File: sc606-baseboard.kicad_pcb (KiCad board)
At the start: 6 copper layers, 100 x 90 mm, 465 parts, among them IC1 TPS54561DPRT, IC2 TPS7A0518PDBVT, IC3 HD3SS3220, IC4 HD3SS3220, J1 PJ-202A, J10 WE_632723300011, J11 USB-A3-C31-D-RA-CS1, J12 U_FL-R-SMT-1_10_, J13 USB-A3-C31-D-RA-CS1, J2 WE_68715014522, J3 F52R-1A7H1-11020, J4 46756-1001, J5 U_FL-R-SMT-1_10_, J6 U_FL-R-SMT-1_10_, J7 DM3AT-SF-PEJM5, J8 693022010811, J9 0473460001, M1 SC606T, Q1 BSS138APW, Q2 BSS138-7-F, Q3 BSS138APW, Q4 BSS138APW, Q5 BSS138APW, Q6 BSS138APW, Q7 BSS138-7-F, Q8 BSS138-7-F, SW1 1X03, U1 AP62301WU-7, U10 NCP163ASN330T1G, U11 EMIF06-MSD02N16, U12 FSUSB30MUX, U13 FT232RQ-REEL, U15 USB57442G, U2 AP62301WU-7, U3 AP62301WU-7, U4 74LVC1G123GN, U5 NTS0102GT, U6 PCA9547BS, U7 LT9611UXC, U8 NTS0102GT, U9 TPD13S523PWR, Y1 ABM8G-24.000MHZ-18-D2Y-T, Y2 ABM8G-25.000MHZ-B4Y-T

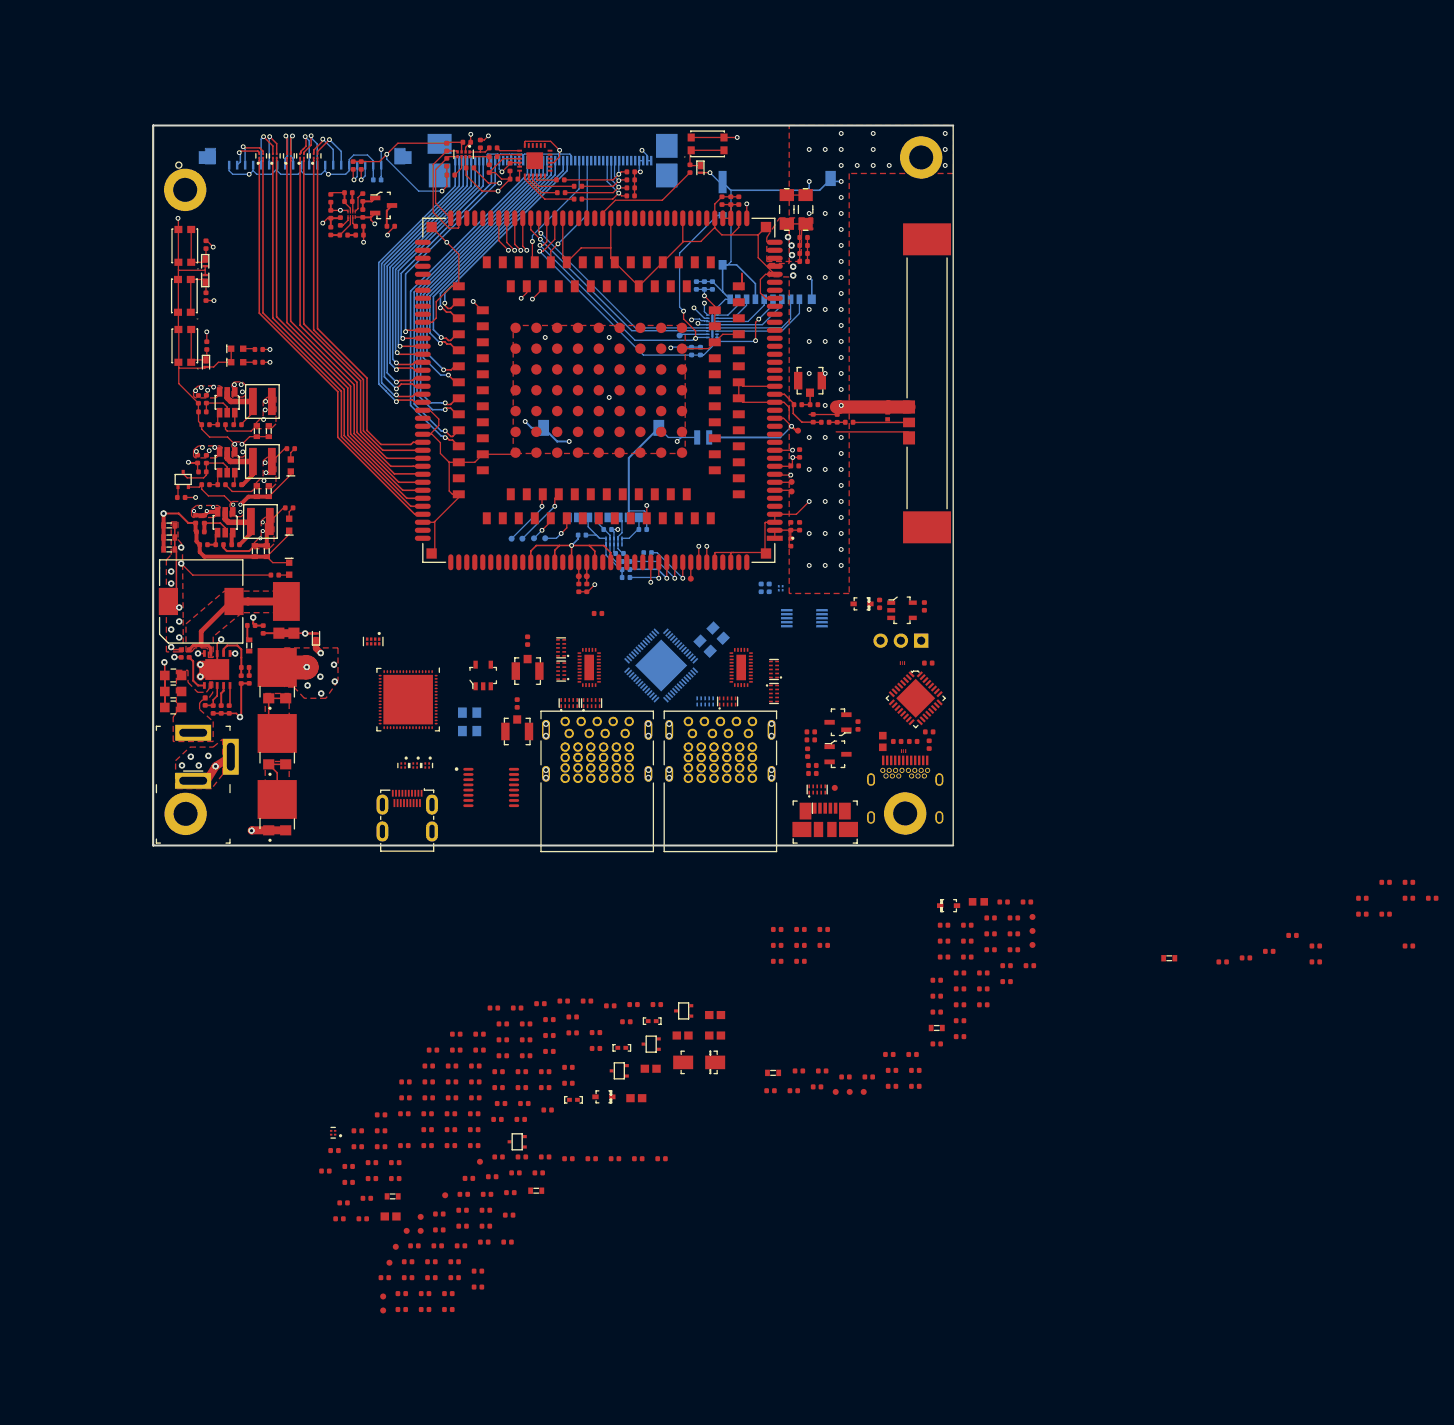
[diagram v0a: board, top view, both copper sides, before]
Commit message: Started rearrangement of components. USB connectors changed to 2xUSB-C
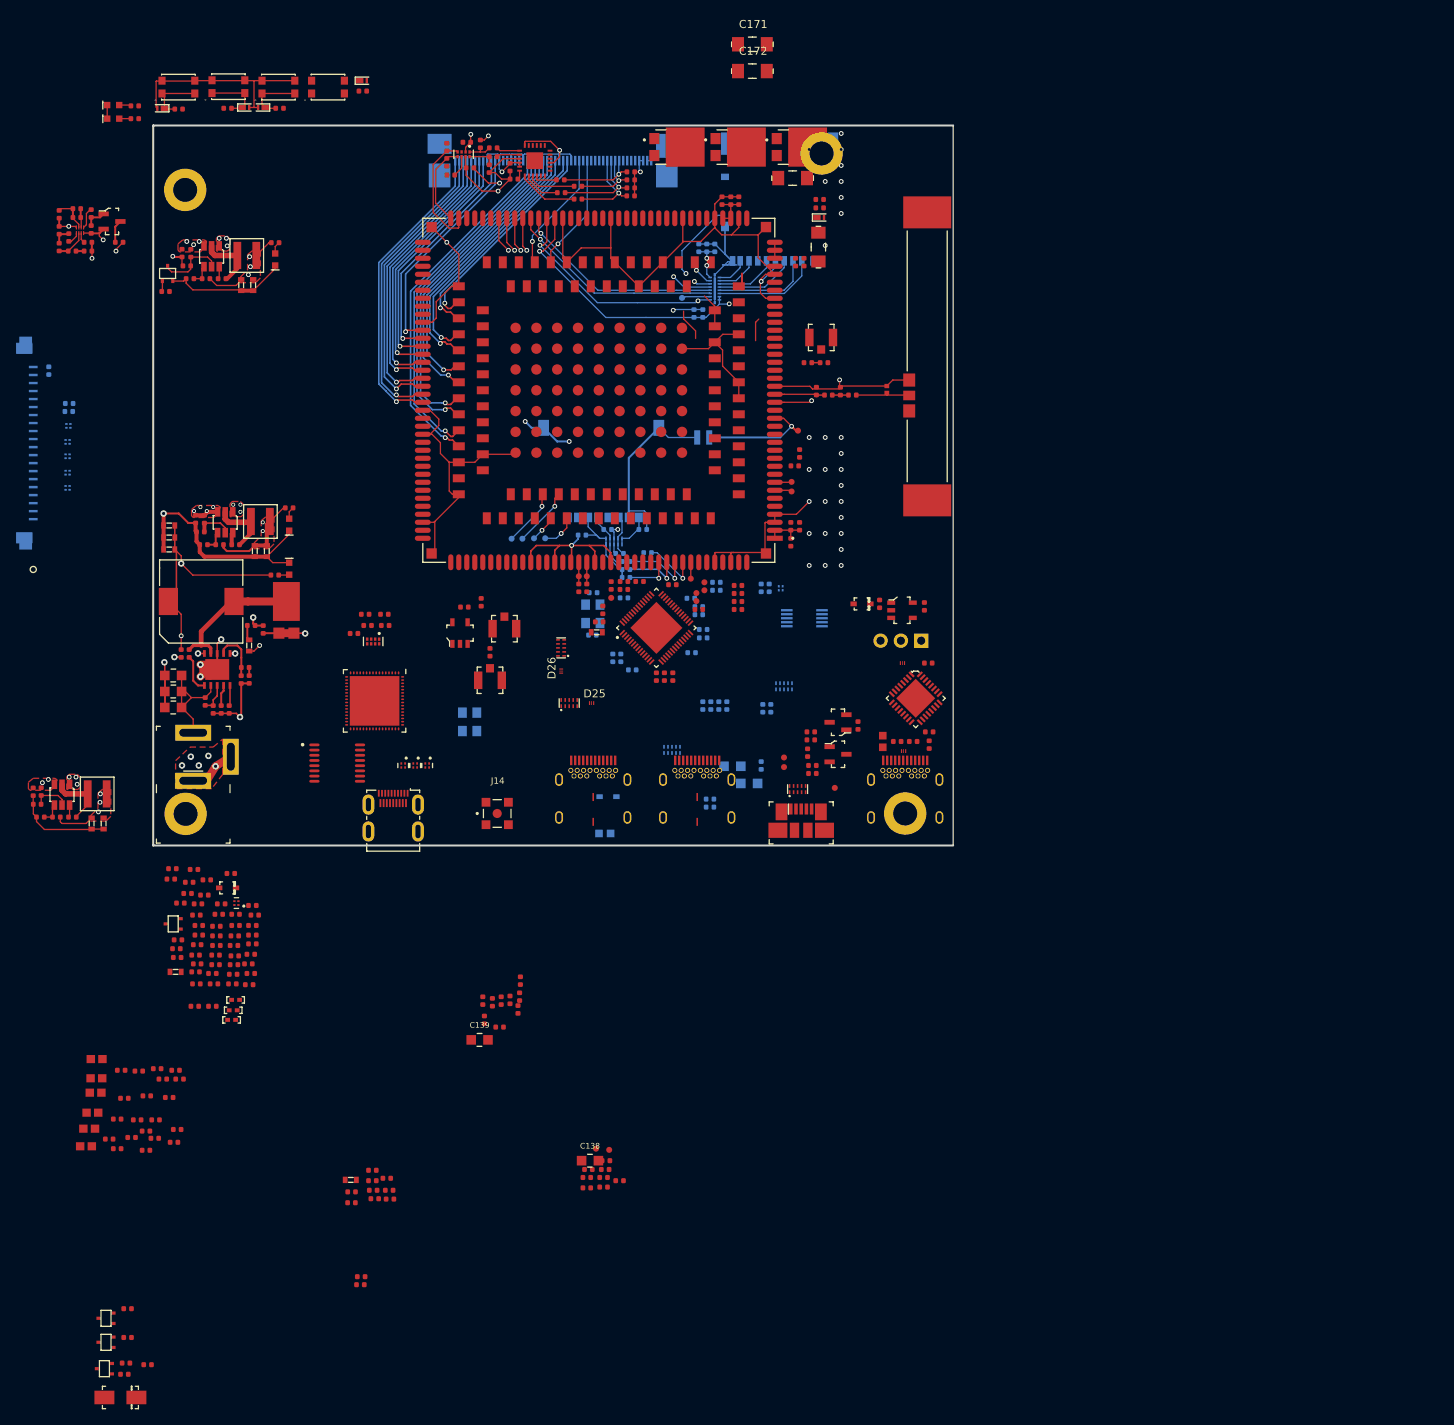
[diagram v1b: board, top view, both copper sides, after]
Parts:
- removed C142, C143, C144, C145, C153, C154, C155, C156, C157, C159, C160, C161, C162, C163, C164, C165, C166: C_100n_0402, sc606-baseboard-footprints:0402-cap
- removed C146, C158: C_47u_0603, sc606-baseboard-footprints:0603-cap
- removed C152: C_10u_0402, sc606-baseboard-footprints:0402-cap
- removed D29, D30: PUSB3F96X_PASS, sc606-baseboard-footprints:PUSB3F96X
- removed IC3, IC4: HD3SS3220, sc606-baseboard-footprints:RNH0030A
- removed R138, R143, R147, R148, R149, R150, R151, R152, R161: R_0R_0402, sc606-baseboard-footprints:0402-res
- removed R139, R140, R146, R153, R154: R_2k_0402, sc606-baseboard-footprints:0402-res
- removed R141, R159: R_909k_0402, sc606-baseboard-footprints:0402-res
- removed R142, R144, R160: R_200k_0402, sc606-baseboard-footprints:0402-res
- removed R145: R_10k_0402, sc606-baseboard-footprints:0402-res
- removed TP20, TP21, TP22, TP25, TP26, TP27: TP_SMD_0_75MM, sc606-baseboard-footprints:Testpoint_smd_0_75mm
- added C169: C_100u_0805, sc606-baseboard-footprints:0805-cap, B.Cu at (149.5, 122.2)
- added C170: C_100u_0805, sc606-baseboard-footprints:0805-cap, B.Cu at (147.4, 120.1)
- added C171: C_100u_1206, sc606-baseboard-footprints:1206-cap, F.Cu at (149.9, 29.9)
- added C172: C_100u_1206, sc606-baseboard-footprints:1206-cap, F.Cu at (149.9, 33.2)
- added J14: CONMMCX002-SMD-T, sc606-baseboard-footprints:LINX_CONMMCX002-SMD-T, F.Cu at (118.0, 126.0)
- C121, C122, C123, C124, C127, C129, C132, C133, C134, C135, C136, C137, C147, C148, C149, C150, C151, D24, D31, D32, FB2, L10, L11, L12, L8, L9, R119, R120, R155, R156, R157, R158, R55, R56: moved to B.Cu
- C138: value C_100n_0402 -> C_100u_0805; footprint sc606-baseboard-footprints:0402-cap -> sc606-baseboard-footprints:0805-cap
- C139: value C_10u_0402 -> C_100u_0805; footprint sc606-baseboard-footprints:0402-cap -> sc606-baseboard-footprints:0805-cap
- D25, D26: value PUSB3F96X_PASS -> PESD5V0C2BDFZ; footprint sc606-baseboard-footprints:PUSB3F96X -> sc606-baseboard-footprints:DFN0603-3
- J11, J13: value USB-A3-C31-D-RA-CS1 -> WE_632723300011; footprint sc606-baseboard-footprints:USB-A3-C31-D-RA-CS1 -> sc606-baseboard-footprints:WE_632723300011
- R130: value R_200k_0402 -> R_0R_0402
- R131: value R_10k_0402 -> R_0R_0402
- R132: value R_2k_0402 -> R_0R_0402
- R162: footprint antmicro-footprints:0402-res -> sc606-baseboard-footprints:0402-res
- U15: moved to F.Cu
- moved C89 135.8 mm to (101.0, 183.9)
- moved C91 134.2 mm to (100.9, 184.9)
- moved C96 133.2 mm to (104.5, 173.1)
- moved C93 132.8 mm to (104.6, 174.2)
- moved C87 130.2 mm to (104.2, 171.6)
- moved C95 127.8 mm to (102.4, 170.6)
- moved C101 121.5 mm to (102.4, 171.9)
- moved C98 119.2 mm to (102.5, 173.1)
- moved C99 118.6 mm to (99.8, 173.3)
- moved C103 114.1 mm to (118.3, 152.7)
- moved R93 113.0 mm to (99.8, 174.7)
- moved R92 113.0 mm to (102.7, 174.2)
- moved C94 110.8 mm to (129.4, 170.5)
- moved R94 106.0 mm to (99.7, 171.8)
- moved D3 96.5 mm to (140.5, 42.7), turned to 270 degrees
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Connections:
- C102 pad 1: /USB_HUB_Connectors/USB_C1_SS_C_TX2_N -> /USB_HUB_Connectors/USB_C1_SS_C_TX1_N
- C102 pad 2: /USB_HUB_Connectors/USB_C1_SS_TX2_N -> /USB_HUB_Connectors/USB_C1_SS_TX1_N
- C103 pad 2: /USB_HUB_Connectors/5V0_USB -> Net-(C103-Pad2)
- C138 pad 1: /USB_HUB_Connectors/USB_C1_SS_C_TX1_P -> GND
- C138 pad 2: /USB_HUB_Connectors/USB_C1_SS_TX1_P -> Net-(C103-Pad2)
- C139 pad 1: /USB_HUB_Connectors/5V0_USB -> GND
- C139 pad 2: GND -> Net-(C103-Pad2)
- C140 pad 1: Net-(C140-Pad1) -> /USB_HUB_Connectors/USB_C1_SS_C_TX2_N
- C140 pad 2: /USB_HUB_Connectors/USB_C1_SS_RX2_N -> /USB_HUB_Connectors/USB_C1_SS_TX2_N
- C141 pad 1: /USB_HUB_Connectors/USB_C1_SS_C_TX1_N -> /USB_HUB_Connectors/USB_C1_SS_C_TX2_P
- C141 pad 2: /USB_HUB_Connectors/USB_C1_SS_TX1_N -> /USB_HUB_Connectors/USB_C1_SS_TX2_P
- C151 pad 2: /USB_HUB_Connectors/5V0_USB -> Net-(C151-Pad2)
- C94 pad 1: /USB_HUB_Connectors/USB_C1_SS_C_TX2_P -> /USB_HUB_Connectors/USB_C1_SS_C_TX1_P
- C94 pad 2: /USB_HUB_Connectors/USB_C1_SS_TX2_P -> /USB_HUB_Connectors/USB_C1_SS_TX1_P
- D25 pad 1: /USB_HUB_Connectors/USB_A1_SS_TX_P -> /USB_HUB_Connectors/USB_C1_D_P
- D25 pad 2: /USB_HUB_Connectors/USB_A1_SS_TX_N -> /USB_HUB_Connectors/USB_C1_D_N
- D26 pad 1: /USB_HUB_Connectors/USB_C1_D_P -> /USB_HUB_Connectors/USB_C2_D_P
- D26 pad 2: /USB_HUB_Connectors/USB_C1_D_N -> /USB_HUB_Connectors/USB_C2_D_N
- D31 pad 1: /USB_HUB_Connectors/USB_C2_SS_RX2_P -> /USB_HUB_Connectors/USB_C2_SS_TX2_P
- D31 pad 10: /USB_HUB_Connectors/USB_C2_SS_RX2_P -> /USB_HUB_Connectors/USB_C2_SS_TX2_P
- D31 pad 2: /USB_HUB_Connectors/USB_C2_SS_RX2_N -> /USB_HUB_Connectors/USB_C2_SS_TX2_N
- D31 pad 4: /USB_HUB_Connectors/USB_C2_SS_TX2_P -> /USB_HUB_Connectors/USB_C2_SS_RX2_P
- D31 pad 5: /USB_HUB_Connectors/USB_C2_SS_TX2_N -> /USB_HUB_Connectors/USB_C2_SS_RX2_N
- D31 pad 6: /USB_HUB_Connectors/USB_C2_SS_TX2_N -> /USB_HUB_Connectors/USB_C2_SS_RX2_N
- D31 pad 7: /USB_HUB_Connectors/USB_C2_SS_TX2_P -> /USB_HUB_Connectors/USB_C2_SS_RX2_P
- D31 pad 9: /USB_HUB_Connectors/USB_C2_SS_RX2_N -> /USB_HUB_Connectors/USB_C2_SS_TX2_N
- D6 pad 2: /display module/SCL_HDMI -> /display module/LTtoHDMI_SCL
- D7 pad 2: /display module/SDA_HDMI -> /display module/LTtoHDMI_SDA
- D8 pad 2: /display module/CEC -> (no net)
- J10 pad A10: Net-(J10-PadA10) -> (no net)
- J10 pad A11: Net-(J10-PadA11) -> (no net)
- J10 pad A2: Net-(J10-PadA2) -> (no net)
- J10 pad A3: Net-(J10-PadA3) -> (no net)
- J10 pad A5: Net-(J10-PadA5) -> (no net)
- J10 pad A8: Net-(J10-PadA8) -> (no net)
- J10 pad B10: Net-(J10-PadB10) -> (no net)
- J10 pad B11: Net-(J10-PadB11) -> (no net)
- J10 pad B2: Net-(J10-PadB2) -> (no net)
- J10 pad B3: Net-(J10-PadB3) -> (no net)
- J10 pad B5: Net-(J10-PadB5) -> (no net)
- J10 pad B8: Net-(J10-PadB8) -> (no net)
- J11 pad A1: GND -> (no net)
- J11 pad A10: Net-(C140-Pad1) -> /USB_HUB_Connectors/USB_C1_SS_C_RX2_N
- J11 pad A11: Net-(C143-Pad1) -> /USB_HUB_Connectors/USB_C1_SS_C_RX2_P
- J11 pad B1: GND -> Net-(C103-Pad2)
- J11 pad B10: Net-(C142-Pad1) -> /USB_HUB_Connectors/USB_C1_SS_C_RX1_P
- J11 pad B11: Net-(C144-Pad1) -> /USB_HUB_Connectors/USB_C1_SS_C_RX1_N
- J11 pad B12: GND -> (no net)
- J13 pad A1: GND -> (no net)
- J13 pad B1: GND -> Net-(C151-Pad2)
- J13 pad B10: /USB_HUB_Connectors/USB_C2_SS_C_RX1_N -> /USB_HUB_Connectors/USB_C2_SS_C_RX1_P
- J13 pad B11: /USB_HUB_Connectors/USB_C2_SS_C_RX1_P -> /USB_HUB_Connectors/USB_C2_SS_C_RX1_N
- J13 pad B12: GND -> (no net)
- J2 pad 13: Net-(J2-Pad13) -> (no net)
- J2 pad 14: Net-(J2-Pad14) -> (no net)
- J2 pad 16: Net-(J2-Pad16) -> (no net)
- J2 pad 17: Net-(J2-Pad17) -> (no net)
- J2 pad 31: Net-(J2-Pad31) -> (no net)
- J2 pad 33: Net-(J2-Pad33) -> (no net)
- J2 pad 35: Net-(J2-Pad35) -> (no net)
- J2 pad 36: Net-(J2-Pad36) -> (no net)
- J2 pad 37: Net-(J2-Pad37) -> (no net)
- J2 pad 38: Net-(J2-Pad38) -> (no net)
- J2 pad 43: Net-(J2-Pad43) -> (no net)
- J2 pad 44: Net-(J2-Pad44) -> (no net)
- J2 pad 45: Net-(J2-Pad45) -> (no net)
- J2 pad 46: Net-(J2-Pad46) -> (no net)
- J8 pad C4: Net-(J8-PadC4) -> (no net)
- J8 pad C6: Net-(J8-PadC6) -> (no net)
- J8 pad C8: Net-(J8-PadC8) -> (no net)
- L10 pad 1: SoMtoDisplay_D1_N -> SoMtoDisplay_D1_P
- L10 pad 2: /display module/SoMtoDisplay_Ferr_D1_N -> /display module/SoMtoDisplay_Ferr_D1_P
- L10 pad 3: /display module/SoMtoDisplay_Ferr_D1_P -> /display module/SoMtoDisplay_Ferr_D1_N
- L10 pad 4: SoMtoDisplay_D1_P -> SoMtoDisplay_D1_N
- L11 pad 1: SoMtoDisplay_D0_N -> SoMtoDisplay_D0_P
- L11 pad 2: /display module/SoMtoDisplay_Ferr_D0_N -> /display module/SoMtoDisplay_Ferr_D0_P
- L11 pad 3: /display module/SoMtoDisplay_Ferr_D0_P -> /display module/SoMtoDisplay_Ferr_D0_N
- L11 pad 4: SoMtoDisplay_D0_P -> SoMtoDisplay_D0_N
- L12 pad 1: SoMtoDisplay_CLK_N -> SoMtoDisplay_CLK_P
- L12 pad 2: /display module/SoMtoDisplay_Ferr_CLK_N -> /display module/SoMtoDisplay_Ferr_CLK_P
- L12 pad 3: /display module/SoMtoDisplay_Ferr_CLK_P -> /display module/SoMtoDisplay_Ferr_CLK_N
- L12 pad 4: SoMtoDisplay_CLK_P -> SoMtoDisplay_CLK_N
- L8 pad 1: SoMtoDisplay_D3_N -> SoMtoDisplay_D3_P
- L8 pad 2: /display module/SoMtoDisplay_Ferr_D3_N -> /display module/SoMtoDisplay_Ferr_D3_P
- L8 pad 3: /display module/SoMtoDisplay_Ferr_D3_P -> /display module/SoMtoDisplay_Ferr_D3_N
- L8 pad 4: SoMtoDisplay_D3_P -> SoMtoDisplay_D3_N
- L9 pad 1: SoMtoDisplay_D2_N -> SoMtoDisplay_D2_P
- L9 pad 2: /display module/SoMtoDisplay_Ferr_D2_N -> /display module/SoMtoDisplay_Ferr_D2_P
- L9 pad 3: /display module/SoMtoDisplay_Ferr_D2_P -> /display module/SoMtoDisplay_Ferr_D2_N
- L9 pad 4: SoMtoDisplay_D2_P -> SoMtoDisplay_D2_N
- M1 pad 100: Net-(M1-Pad100) -> (no net)
- M1 pad 11: LDO10_2P8 -> (no net)
- M1 pad 113: Net-(M1-Pad113) -> (no net)
- M1 pad 114: Net-(M1-Pad114) -> (no net)
- M1 pad 126: Net-(M1-Pad126) -> (no net)
- M1 pad 127: Net-(M1-Pad127) -> (no net)
- M1 pad 13: Net-(M1-Pad13) -> (no net)
- M1 pad 136: Net-(M1-Pad136) -> (no net)
- M1 pad 137: Net-(M1-Pad137) -> (no net)
- M1 pad 138: Net-(M1-Pad138) -> (no net)
- M1 pad 139: Net-(M1-Pad139) -> (no net)
- M1 pad 14: Net-(M1-Pad14) -> (no net)
- M1 pad 149: Net-(M1-Pad149) -> (no net)
- M1 pad 15: Net-(M1-Pad15) -> (no net)
- M1 pad 151: Net-(M1-Pad151) -> (no net)
- M1 pad 152: Net-(M1-Pad152) -> (no net)
- M1 pad 153: Net-(M1-Pad153) -> (no net)
- M1 pad 154: Net-(M1-Pad154) -> (no net)
- M1 pad 155: Net-(M1-Pad155) -> (no net)
- M1 pad 156: Net-(M1-Pad156) -> (no net)
- M1 pad 157: Net-(M1-Pad157) -> (no net)
- M1 pad 158: Net-(M1-Pad158) -> (no net)
- M1 pad 161: Net-(M1-Pad161) -> (no net)
- M1 pad 162: Net-(M1-Pad162) -> (no net)
- M1 pad 164: Net-(M1-Pad164) -> (no net)
- M1 pad 165: Net-(M1-Pad165) -> (no net)
- M1 pad 166: Net-(M1-Pad166) -> (no net)
- M1 pad 167: Net-(M1-Pad167) -> (no net)
- M1 pad 168: Net-(M1-Pad168) -> (no net)
- M1 pad 169: Net-(M1-Pad169) -> (no net)
- M1 pad 17: Net-(M1-Pad17) -> (no net)
- M1 pad 179: Net-(M1-Pad179) -> (no net)
- M1 pad 180: Net-(M1-Pad180) -> (no net)
- M1 pad 181: Net-(M1-Pad181) -> (no net)
- M1 pad 194: Net-(M1-Pad194) -> (no net)
- M1 pad 196: Net-(M1-Pad196) -> (no net)
- M1 pad 197: Net-(M1-Pad197) -> (no net)
- M1 pad 198: Net-(M1-Pad198) -> (no net)
- M1 pad 199: Net-(M1-Pad199) -> (no net)
- M1 pad 202: Net-(M1-Pad202) -> (no net)
- M1 pad 203: Net-(M1-Pad203) -> (no net)
- M1 pad 207: Net-(M1-Pad207) -> (no net)
- M1 pad 208: Net-(M1-Pad208) -> (no net)
- M1 pad 209: Net-(M1-Pad209) -> (no net)
- M1 pad 21: Net-(M1-Pad21) -> (no net)
- M1 pad 210: Net-(M1-Pad210) -> (no net)
- M1 pad 211: Net-(M1-Pad211) -> (no net)
- M1 pad 212: Net-(M1-Pad212) -> (no net)
- M1 pad 213: Net-(M1-Pad213) -> (no net)
- M1 pad 214: Net-(M1-Pad214) -> (no net)
- M1 pad 215: Net-(M1-Pad215) -> (no net)
- M1 pad 216: Net-(M1-Pad216) -> (no net)
- M1 pad 217: Net-(M1-Pad217) -> (no net)
- M1 pad 218: Net-(M1-Pad218) -> (no net)
- M1 pad 22: Net-(M1-Pad22) -> (no net)
- M1 pad 222: Net-(M1-Pad222) -> (no net)
- M1 pad 223: Net-(M1-Pad223) -> (no net)
- M1 pad 224: Net-(M1-Pad224) -> (no net)
- M1 pad 226: Net-(M1-Pad226) -> (no net)
- M1 pad 227: Net-(M1-Pad227) -> (no net)
- M1 pad 228: Net-(M1-Pad228) -> (no net)
- M1 pad 23: Net-(M1-Pad23) -> (no net)
- M1 pad 233: Net-(M1-Pad233) -> (no net)
- M1 pad 235: Net-(M1-Pad235) -> (no net)
- M1 pad 236: Net-(M1-Pad236) -> (no net)
- M1 pad 237: Net-(M1-Pad237) -> (no net)
- M1 pad 238: Net-(M1-Pad238) -> (no net)
- M1 pad 239: Net-(M1-Pad239) -> (no net)
- M1 pad 24: Net-(M1-Pad24) -> (no net)
- M1 pad 240: Net-(M1-Pad240) -> (no net)
- M1 pad 241: Net-(M1-Pad241) -> (no net)
- M1 pad 242: Net-(M1-Pad242) -> (no net)
- M1 pad 244: Net-(M1-Pad244) -> (no net)
- M1 pad 245: Net-(M1-Pad245) -> (no net)
- M1 pad 246: Net-(M1-Pad246) -> (no net)
- M1 pad 249: Net-(M1-Pad249) -> (no net)
- M1 pad 25: Net-(M1-Pad25) -> (no net)
- M1 pad 250: Net-(M1-Pad250) -> (no net)
- M1 pad 251: Net-(M1-Pad251) -> (no net)
- M1 pad 252: Net-(M1-Pad252) -> (no net)
- M1 pad 253: Net-(M1-Pad253) -> (no net)
- M1 pad 254: Net-(M1-Pad254) -> (no net)
- M1 pad 255: Net-(M1-Pad255) -> (no net)
- M1 pad 256: Net-(M1-Pad256) -> (no net)
- M1 pad 26: Net-(M1-Pad26) -> (no net)
- M1 pad 27: Net-(M1-Pad27) -> (no net)
- M1 pad 28: Net-(M1-Pad28) -> (no net)
- M1 pad 29: Net-(M1-Pad29) -> (no net)
- M1 pad 44: Net-(M1-Pad44) -> (no net)
- M1 pad 45: Net-(M1-Pad45) -> (no net)
- M1 pad 46: Net-(M1-Pad46) -> (no net)
- M1 pad 48: Net-(M1-Pad48) -> (no net)
- M1 pad 49: Net-(M1-Pad49) -> (no net)
- M1 pad 50: Net-(M1-Pad50) -> (no net)
- M1 pad 51: Net-(M1-Pad51) -> (no net)
- M1 pad 52: Net-(M1-Pad52) -> (no net)
- M1 pad 53: Net-(M1-Pad53) -> (no net)
- M1 pad 54: Net-(M1-Pad54) -> (no net)
- M1 pad 55: Net-(M1-Pad55) -> (no net)
- M1 pad 58: Net-(M1-Pad58) -> (no net)
- M1 pad 59: Net-(M1-Pad59) -> (no net)
- M1 pad 60: Net-(M1-Pad60) -> (no net)
- M1 pad 61: Net-(M1-Pad61) -> (no net)
- M1 pad 71: Net-(M1-Pad71) -> (no net)
- M1 pad 72: Net-(M1-Pad72) -> (no net)
- M1 pad 73: Net-(M1-Pad73) -> (no net)
- M1 pad 74: Net-(M1-Pad74) -> (no net)
- M1 pad 77: Net-(M1-Pad77) -> (no net)
- M1 pad 78: Net-(M1-Pad78) -> (no net)
- M1 pad 79: Net-(M1-Pad79) -> (no net)
- M1 pad 80: Net-(M1-Pad80) -> (no net)
- M1 pad 81: Net-(M1-Pad81) -> (no net)
- M1 pad 82: Net-(M1-Pad82) -> (no net)
- M1 pad 83: Net-(M1-Pad83) -> (no net)
- M1 pad 84: Net-(M1-Pad84) -> (no net)
- M1 pad 85: Net-(M1-Pad85) -> (no net)
- M1 pad 86: Net-(M1-Pad86) -> (no net)
- M1 pad 99: Net-(M1-Pad99) -> (no net)
- R122 pad 1: /USB_HUB_Connectors/USB_C1_CC1 -> /USB_HUB_Connectors/USB_C1_SS_RX2_P
- R122 pad 2: Net-(J11-PadB5) -> /USB_HUB_Connectors/USB_C1_SS_C_RX2_P
- R123 pad 2: Net-(J11-PadB5) -> Net-(J11-PadA5)
- R124 pad 1: /USB_HUB_Connectors/USB_C1_CC2 -> /USB_HUB_Connectors/USB_C1_SS_RX2_N
- R124 pad 2: Net-(J11-PadA5) -> /USB_HUB_Connectors/USB_C1_SS_C_RX2_N
- R130 pad 1: 5V0_SYS -> /USB_HUB_Connectors/USB_C1_SS_RX1_N
- R130 pad 2: Net-(IC3-Pad23) -> /USB_HUB_Connectors/USB_C1_SS_C_RX1_N
- R131 pad 1: 5V0_SYS -> /USB_HUB_Connectors/USB_C1_CC1
- R131 pad 2: Net-(IC3-Pad3) -> Net-(J11-PadB5)
- R132 pad 1: 5V0_SYS -> /USB_HUB_Connectors/USB_C1_CC2
- R132 pad 2: Net-(IC3-Pad4) -> Net-(J11-PadB5)
- R133 pad 1: GND -> /USB_HUB_Connectors/USB_C1_SS_RX1_P
- R133 pad 2: /USB_HUB_Connectors/EN1_MUX -> /USB_HUB_Connectors/USB_C1_SS_C_RX1_P
- R134 pad 1: GND -> /USB_HUB_Connectors/USB_C2_SS_RX2_P
- R134 pad 2: Net-(IC3-Pad29) -> /USB_HUB_Connectors/USB_C2_SS_C_RX2_P
- R135 pad 1: /USB_HUB_Connectors/USB_C1_SS_TX_P -> /USB_HUB_Connectors/USB_C2_SS_RX2_N
- R135 pad 2: /USB_HUB_Connectors/USB_C1_SS_C_TX_P -> /USB_HUB_Connectors/USB_C2_SS_C_RX2_N
- R136 pad 1: /USB_HUB_Connectors/USB_C1_SS_TX_N -> /USB_HUB_Connectors/USB_C2_SS_RX1_N
- R136 pad 2: /USB_HUB_Connectors/USB_C1_SS_C_TX_N -> /USB_HUB_Connectors/USB_C2_SS_C_RX1_N
- R137 pad 1: /USB_HUB_Connectors/USB_C1_SS_RX_P -> /USB_HUB_Connectors/USB_C2_SS_RX1_P
- R137 pad 2: /USB_HUB_Connectors/USB_C1_SS_C_RX_P -> /USB_HUB_Connectors/USB_C2_SS_C_RX1_P
- R155 pad 1: /USB_HUB_Connectors/USB_C2_CC2 -> /USB_HUB_Connectors/USB_C2_CC1
- R155 pad 2: Net-(J13-PadA5) -> Net-(J13-PadB5)
- R158 pad 1: /USB_HUB_Connectors/USB_C2_CC1 -> /USB_HUB_Connectors/USB_C2_CC2
- R158 pad 2: Net-(J13-PadB5) -> Net-(J13-PadA5)
- R61 pad 2: /display module/SCL_HDMI -> /display module/LTtoHDMI_SCL
- R62 pad 2: /display module/SDA_HDMI -> /display module/LTtoHDMI_SDA
- U13 pad 10: Net-(U13-Pad10) -> (no net)
- U13 pad 11: Net-(U13-Pad11) -> (no net)
- U13 pad 12: Net-(U13-Pad12) -> (no net)
- U13 pad 13: Net-(U13-Pad13) -> (no net)
- U13 pad 18: Net-(U13-Pad18) -> (no net)
- U13 pad 21: Net-(U13-Pad21) -> (no net)
- U13 pad 22: Net-(U13-Pad22) -> (no net)
- U13 pad 23: Net-(U13-Pad23) -> (no net)
- U13 pad 25: Net-(U13-Pad25) -> (no net)
- U13 pad 27: Net-(U13-Pad27) -> (no net)
- U13 pad 28: Net-(U13-Pad28) -> (no net)
- U13 pad 29: Net-(U13-Pad29) -> (no net)
- U13 pad 3: Net-(U13-Pad3) -> (no net)
- U13 pad 31: Net-(U13-Pad31) -> (no net)
- U13 pad 32: Net-(U13-Pad32) -> (no net)
- U13 pad 5: Net-(U13-Pad5) -> (no net)
- U13 pad 6: Net-(U13-Pad6) -> (no net)
- U13 pad 7: Net-(U13-Pad7) -> (no net)
- U13 pad 8: Net-(U13-Pad8) -> (no net)
- U13 pad 9: Net-(U13-Pad9) -> (no net)
- U15 pad 1: /USB_HUB_Connectors/USB_A1_D_P -> /USB_HUB_Connectors/USB_C1_D_P
- U15 pad 10: /USB_HUB_Connectors/USB_C1_SS_TX_P -> /USB_HUB_Connectors/USB_C1_SS_TX2_P
- U15 pad 11: /USB_HUB_Connectors/USB_C1_SS_TX_N -> /USB_HUB_Connectors/USB_C1_SS_TX2_N
- U15 pad 13: /USB_HUB_Connectors/USB_C1_SS_RX_P -> /USB_HUB_Connectors/USB_C1_SS_RX2_P
- U15 pad 14: /USB_HUB_Connectors/USB_C1_SS_RX_N -> /USB_HUB_Connectors/USB_C1_SS_RX2_N
- U15 pad 17: /USB_HUB_Connectors/USB_A2_D_P -> /USB_HUB_Connectors/USB_C2_D_P
- U15 pad 18: /USB_HUB_Connectors/USB_A2_D_N -> /USB_HUB_Connectors/USB_C2_D_N
- U15 pad 19: /USB_HUB_Connectors/USB_A2_SS_TX_P -> /USB_HUB_Connectors/USB_C2_SS_TX1_P
- U15 pad 2: /USB_HUB_Connectors/USB_A1_D_N -> /USB_HUB_Connectors/USB_C1_D_N
- U15 pad 20: /USB_HUB_Connectors/USB_A2_SS_TX_N -> /USB_HUB_Connectors/USB_C2_SS_TX1_N
- U15 pad 22: /USB_HUB_Connectors/USB_A2_SS_RX_P -> /USB_HUB_Connectors/USB_C2_SS_RX1_P
- U15 pad 23: /USB_HUB_Connectors/USB_A2_SS_RX_N -> /USB_HUB_Connectors/USB_C2_SS_RX1_N
- U15 pad 26: /USB_HUB_Connectors/USB_C2_SS_TX_P -> /USB_HUB_Connectors/USB_C2_SS_TX2_P
- U15 pad 27: /USB_HUB_Connectors/USB_C2_SS_TX_N -> /USB_HUB_Connectors/USB_C2_SS_TX2_N
- U15 pad 29: /USB_HUB_Connectors/USB_C2_SS_RX_P -> /USB_HUB_Connectors/USB_C2_SS_RX2_N
- U15 pad 3: /USB_HUB_Connectors/USB_A1_SS_TX_P -> /USB_HUB_Connectors/USB_C1_SS_TX1_P
- U15 pad 30: /USB_HUB_Connectors/USB_C2_SS_RX_N -> /USB_HUB_Connectors/USB_C2_SS_RX2_P
- U15 pad 4: /USB_HUB_Connectors/USB_A1_SS_TX_N -> /USB_HUB_Connectors/USB_C1_SS_TX1_N
- U15 pad 6: /USB_HUB_Connectors/USB_A1_SS_RX_P -> /USB_HUB_Connectors/USB_C1_SS_RX1_P
- U15 pad 7: /USB_HUB_Connectors/USB_A1_SS_RX_N -> /USB_HUB_Connectors/USB_C1_SS_RX1_N
- U6 pad 10: Net-(U6-Pad10) -> (no net)
- U6 pad 11: Net-(U6-Pad11) -> (no net)
- U6 pad 12: Net-(U6-Pad12) -> (no net)
- U6 pad 13: Net-(U6-Pad13) -> (no net)
- U6 pad 14: Net-(U6-Pad14) -> (no net)
- U6 pad 15: Net-(U6-Pad15) -> (no net)
- U6 pad 16: Net-(U6-Pad16) -> (no net)
- U6 pad 17: Net-(U6-Pad17) -> (no net)
- U6 pad 5: Net-(U6-Pad5) -> (no net)
- U6 pad 6: Net-(U6-Pad6) -> (no net)
- U6 pad 7: Net-(U6-Pad7) -> (no net)
- U6 pad 8: Net-(U6-Pad8) -> (no net)
- U7 pad 1: Net-(U7-Pad1) -> (no net)
- U7 pad 16: Net-(U7-Pad16) -> (no net)
- U7 pad 2: Net-(U7-Pad2) -> (no net)
- U7 pad 20: Net-(U7-Pad20) -> (no net)
- U7 pad 21: Net-(U7-Pad21) -> (no net)
- U7 pad 22: Net-(U7-Pad22) -> (no net)
- U7 pad 27: Net-(U7-Pad27) -> (no net)
- U7 pad 28: Net-(U7-Pad28) -> (no net)
- U7 pad 29: Net-(U7-Pad29) -> (no net)
- U7 pad 30: Net-(U7-Pad30) -> (no net)
- U7 pad 31: Net-(U7-Pad31) -> (no net)
- U7 pad 32: Net-(U7-Pad32) -> (no net)
- U7 pad 33: Net-(U7-Pad33) -> (no net)
- U7 pad 57: Net-(U7-Pad57) -> (no net)
- U7 pad 58: Net-(U7-Pad58) -> (no net)
- U7 pad 59: Net-(U7-Pad59) -> (no net)
- U7 pad 60: Net-(U7-Pad60) -> (no net)
- U7 pad 61: Net-(U7-Pad61) -> (no net)
- U7 pad 62: Net-(U7-Pad62) -> (no net)
- U7 pad 63: Net-(U7-Pad63) -> (no net)
- U7 pad 64: Net-(U7-Pad64) -> (no net)
- U8 pad 1: /display module/SoMtoLT_SDA -> (no net)
- U9 pad 9: Net-(U9-Pad9) -> (no net)
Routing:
- net LDO6_1P8: track 151.5 -> 0.00 mm, vias 4 -> 0
- net LDO17_2P85: track 94.5 -> 0.00 mm, vias 2 -> 0
- net VOL_DOWN: track 91.9 -> 0.00 mm, vias 2 -> 0
- net GND: track 511.9 -> 421.0 mm, vias 102 -> 62
- net V_SOM: track 91.2 -> 2.00 mm, vias 10 -> 2
- net VOL_UP: track 85.8 -> 0.00 mm, vias 2 -> 0
- net 3V3_SYS: track 125.1 -> 43.2 mm, vias 5 -> 4
- net 5V0_SYS: track 142.9 -> 63.9 mm, vias 25 -> 14
- net PWRKEY: track 73.4 -> 1.47 mm, vias 3 -> 1
- net TP0_I2C_SCL: track 71.5 -> 0.00 mm, vias 2 -> 0
- net CAM_RST: track 68.1 -> 0.00 mm, vias 2 -> 0
- net TP0_I2C_SDA: track 60.5 -> 0.00 mm, vias 2 -> 0
- net SoMtoDisplay_D3_N: track 53.6 -> 0.00 mm
- net LDO5_1P8: track 52.8 -> 0.00 mm, vias 2 -> 0
- net SoMtoDisplay_D3_P: track 52.7 -> 0.00 mm
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- removed copper zone on In3.5V0, net 5V0_SYS
- removed copper zone on F.Cu, net Net-(C25-Pad2)
- removed copper zone on F.Cu, net Net-(D3-Pad3)
- removed copper zone on F.Cu, net Net-(D4-Pad3)
- removed copper zone on F.Cu, net VCC
- removed copper zone on F.Cu, net V_SOM
- removed copper zone on In3.5V0, net V_SOM
